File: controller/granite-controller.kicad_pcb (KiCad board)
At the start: 4 copper layers, 199 x 50 mm, 207 parts, among them J1 HR911105A, J10 DRY_IN, J11 MB01_FP, J12 MB02_FP, J13 MB03_FP, J14 MB04_FP, J15 MB05_FP, J16 MB06_FP, J17 MB07_FP, J18 MB08_FP, J2 TYPE-C-31-M-12, J3 19V_IN, J4 1WIRE, J5 1WIRE, J6 1WIRE, J7 1WIRE, J8 EXPANSION, J9 I2C_SENSOR, K1 TLP176AM, K10 TLP176AM, K11 TLP176AM, K12 TLP176AM, K13 TLP176AM, K14 TLP176AM, K15 TLP176AM, K16 TLP176AM, K2 TLP176AM, K3 TLP176AM, K4 TLP176AM, K5 TLP176AM, K6 TLP176AM, K7 TLP176AM, K8 TLP176AM, K9 TLP176AM, U1 ESP32-C6-WROOM-1-N8, U14 MCP23017-E/SO, U15 MCP23017-E/SO, U16 TLP290-4, U17 TLP290-4, U18 TPD4E05U06DQA, U2 TLV62569DBV, U3 W5500, U4 USBLC6-2SC6, U5 TMP1075D, U6 TPD4E05U06DQA, U7 TPD4E05U06DQA, U8 LMR51430YDDCR, Y2 25MHz 12pF YXC

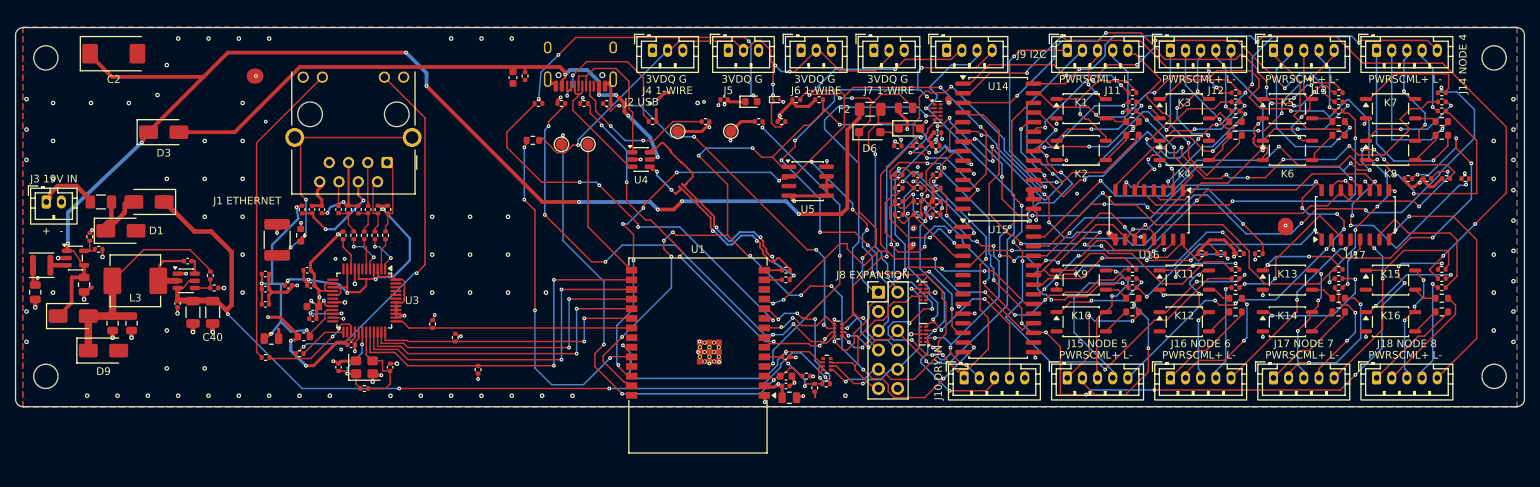
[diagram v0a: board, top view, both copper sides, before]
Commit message: controller rev D: board rebuilt from the rev D schematic and placed, 100 x 50 mm (not routed)
pcbkit mkboard + outline (100 x 50 at rev C's origin, M3 holes in the
corners as rev C), then tools/place.py: ETH (J1 / U3 / Y2 / magnetics,
pairs), buck (U8 loop + U2) and USB-C (J2 / U4) blocks moved from rev C
with their routing (group hand), U1 12 mm left with its decoupling and
antenna still over the bottom edge; probes J4-J7 on the top edge between
RJ45 and USB-C, J11 / J12 (12 V) and J14 / J13 (plane link) on the bottom
edge next to U1's plane I2C pins, J9 / J10 on the right edge. Rule areas:
U1 body, screw heads. Net classes: PWR_19V and node classes gone, PWR_12V
(VIN_12V, 12V_IN_*), LINK?_3V3 in PWR_3V3; pcbkit.toml updated (outline,
classes, labels, KRT nets, keep_groups). DRC parity 0.
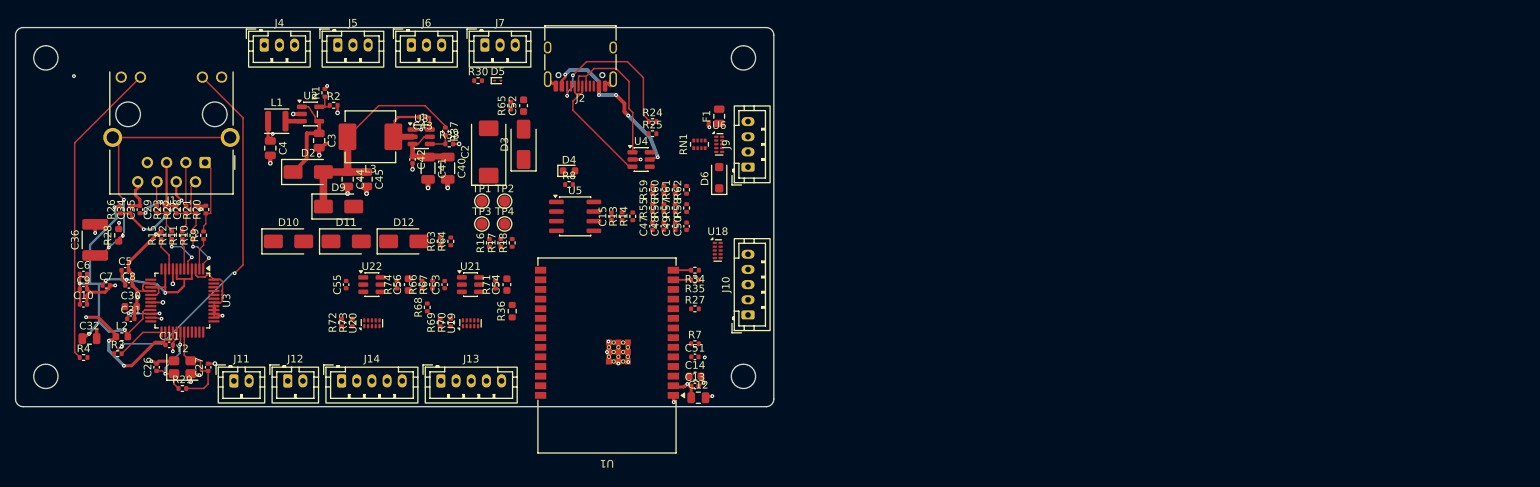
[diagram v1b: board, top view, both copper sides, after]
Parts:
- removed C38, C46: 100n, Capacitor_SMD:C_0402_1005Metric
- removed D1: SMAJ22A, Diode_SMD:D_SMA
- removed D7: SMF5.0A, Diode_SMD:D_SOD-123F
- removed D8: SS34, Diode_SMD:D_SMA
- removed F2: PTC 500mA, Fuse:Fuse_1206_3216Metric
- removed F3: PTC 0.75A, Fuse:Fuse_1206_3216Metric
- removed J15: MB05_FP, Connector_JST:JST_PH_B5B-PH-K_1x05_P2.00mm_Vertical
- removed J16: MB06_FP, Connector_JST:JST_PH_B5B-PH-K_1x05_P2.00mm_Vertical
- removed J17: MB07_FP, Connector_JST:JST_PH_B5B-PH-K_1x05_P2.00mm_Vertical
- removed J18: MB08_FP, Connector_JST:JST_PH_B5B-PH-K_1x05_P2.00mm_Vertical
- removed J3: 19V_IN, Connector_JST:JST_PH_B2B-PH-K_1x02_P2.00mm_Vertical
- removed J8: EXPANSION, Connector_PinHeader_2.54mm:PinHeader_2x06_P2.54mm_Vertical
- removed K1, K10, K11, K12, K13, K14, K15, K16, K2, K3, K4, K5, K6, K7, K8, K9: TLP176AM, Package_SO:SOIC-4_4.55x3.7mm_P2.54mm
- removed R101, R102, R103, R104, R105, R106, R107, R108, R109, R110, R111, R112, R113, R114, R115, R116: 270, Resistor_SMD:R_0402_1005Metric
- removed R19, R32, R33: 10k, Resistor_SMD:R_0402_1005Metric
- removed R201, R202, R203, R204, R205, R206, R207, R208, R209, R210, R211, R212, R213, R214, R215, R216: 100, Resistor_SMD:R_0603_1608Metric
- removed R39, R40, R41, R42, R43, R44, R45, R46: 47k, Resistor_SMD:R_0402_1005Metric
- removed R47, R48, R49, R50, R51, R52, R53, R54: 220, Resistor_SMD:R_0402_1005Metric
- removed R5, R6: 4.7k, Resistor_SMD:R_0402_1005Metric
- removed RN2: 4x330, Resistor_SMD:R_Array_Convex_4x0402
- removed U14, U15: MCP23017-E/SO, Package_SO:SOIC-28W_7.5x17.9mm_P1.27mm
- removed U16, U17: TLP290-4, Package_SO:SOP-16_4.55x10.3mm_P1.27mm
- removed U7: TPD4E05U06DQA, Package_SON:USON-10_2.5x1.0mm_P0.5mm
- added C53: 100n, Capacitor_SMD:C_0402_1005Metric, F.Cu at (81.6, 62.5)
- added C54: 1u, Capacitor_SMD:C_0603_1608Metric, F.Cu at (89.8, 62.5)
- added C55: 100n, Capacitor_SMD:C_0402_1005Metric, F.Cu at (68.6, 62.5)
- added C56: 1u, Capacitor_SMD:C_0603_1608Metric, F.Cu at (76.8, 62.5)
- added D10: SS34, Diode_SMD:D_SMA, F.Cu at (61.0, 56.8)
- added D11: SS34, Diode_SMD:D_SMA, F.Cu at (68.6, 56.8)
- added D12: SMAJ15A, Diode_SMD:D_SMA, F.Cu at (76.2, 56.8)
- added R66: 2.2k, Resistor_SMD:R_0402_1005Metric, F.Cu at (78.6, 62.5)
- added R67: 2.2k, Resistor_SMD:R_0402_1005Metric, F.Cu at (80.0, 62.5)
- added R68: 10k, Resistor_SMD:R_0402_1005Metric, F.Cu at (79.3, 65.5)
- added R69: 33, Resistor_SMD:R_0402_1005Metric, F.Cu at (81.0, 67.5)
- added R70: 33, Resistor_SMD:R_0402_1005Metric, F.Cu at (82.4, 67.5)
- added R71: 180k, Resistor_SMD:R_0402_1005Metric, F.Cu at (88.3, 62.5)
- added R72: 33, Resistor_SMD:R_0402_1005Metric, F.Cu at (68.0, 67.5)
- added R73: 33, Resistor_SMD:R_0402_1005Metric, F.Cu at (69.4, 67.5)
- added R74: 180k, Resistor_SMD:R_0402_1005Metric, F.Cu at (75.3, 62.5)
- added U19: TPD4E05U06DQA, Package_SON:USON-10_2.5x1.0mm_P0.5mm, F.Cu at (85.0, 67.6)
- added U20: TPD4E05U06DQA, Package_SON:USON-10_2.5x1.0mm_P0.5mm, F.Cu at (72.0, 67.6)
- added U21: TPS2553DBVR, Package_TO_SOT_SMD:SOT-23-6, F.Cu at (85.0, 62.5)
- added U22: TPS2553DBVR, Package_TO_SOT_SMD:SOT-23-6, F.Cu at (72.0, 62.5)
- J11: value MB01_FP -> 12V_IN_A; footprint Connector_JST:JST_PH_B5B-PH-K_1x05_P2.00mm_Vertical -> Connector_JST:JST_PH_B2B-PH-K_1x02_P2.00mm_Vertical
- J12: value MB02_FP -> 12V_IN_B; footprint Connector_JST:JST_PH_B5B-PH-K_1x05_P2.00mm_Vertical -> Connector_JST:JST_PH_B2B-PH-K_1x02_P2.00mm_Vertical
- J13: value MB03_FP -> PLANE_LINK_A
- J14: value MB04_FP -> PLANE_LINK_B
- R63: value 100k -> 68k
- moved J14 143.3 mm to (68.0, 75.2)
- moved J12 124.3 mm to (60.9, 75.2)
- moved J11 118.2 mm to (53.8, 75.2)
- moved J13 118.1 mm to (81.1, 75.2)
- moved H2 99.0 mm to (121.0, 32.6)
- moved H3 99.0 mm to (121.0, 74.6)
- moved R63 54.3 mm to (81.0, 56.8), turned to 90 degrees
- moved R64 51.7 mm to (82.4, 56.8), turned to 90 degrees
- moved J5 51.5 mm to (67.5, 30.9)
- moved J6 51.4 mm to (77.2, 30.9)
- moved J7 51.3 mm to (86.9, 30.9)
- moved J4 51.2 mm to (57.8, 30.9)
- moved C2 51.1 mm to (87.4, 45.0), turned to 90 degrees
- moved D3 47.5 mm to (92.0, 44.0), turned to 90 degrees
- moved R30 40.4 mm to (86.0, 35.6)
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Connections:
- net /Expansion header/DRYC1 renamed /Sensors and dry contacts/DRYC1
- net /Expansion header/DRYC2 renamed /Sensors and dry contacts/DRYC2
- net /Expansion header/DRYC3 renamed /Sensors and dry contacts/DRYC3
- net /Expansion header/DRYC4 renamed /Sensors and dry contacts/DRYC4
- net /Expansion header/HDR_3V3 renamed /Sensors and dry contacts/HDR_3V3
- net /Expansion header/HDR_SCL renamed /Sensors and dry contacts/HDR_SCL
- net /Expansion header/HDR_SDA renamed /Sensors and dry contacts/HDR_SDA
- net /Power/VIN_19V renamed /Power/VIN_12V
- J11 pad 1: /Relay channels/MB1_PWR_B -> /Power/12V_IN_A
- J11 pad 2: /Relay channels/MB1_RST_B -> GND
- J12 pad 1: /Relay channels/MB2_PWR_B -> /Power/12V_IN_B
- J12 pad 2: /Relay channels/MB2_RST_B -> GND
- J13 pad 1: /Relay channels/MB3_PWR_B -> /Plane link/LINKA_3V3
- J13 pad 2: /Relay channels/MB3_RST_B -> GND
- J13 pad 3: /Relay channels/MB3_COM -> /Plane link/LINKA_SCL
- J13 pad 4: /Relay channels/MB3_PLED_P -> /Plane link/LINKA_SDA
- J13 pad 5: /Relay channels/MB3_PLED_N -> EXP_INT
- J14 pad 1: /Relay channels/MB4_PWR_B -> /Plane link/LINKB_3V3
- J14 pad 2: /Relay channels/MB4_RST_B -> GND
- J14 pad 3: /Relay channels/MB4_COM -> /Plane link/LINKB_SCL
- J14 pad 4: /Relay channels/MB4_PLED_P -> /Plane link/LINKB_SDA
- J14 pad 5: /Relay channels/MB4_PLED_N -> EXP_INT
- R13 pad 2: I2C_EXT_SCL -> I2C_LOC_SCL
- R14 pad 2: I2C_EXT_SDA -> I2C_LOC_SDA
- RN1 pad 3: /Expansion header/HDR_nRESET -> unconnected-(RN1-R3.1-Pad3)
- RN1 pad 4: /Expansion header/HDR_INT -> unconnected-(RN1-R4.1-Pad4)
- RN1 pad 5: EXP_INT -> unconnected-(RN1-R4.2-Pad5)
- RN1 pad 6: EXP_nRESET -> unconnected-(RN1-R3.2-Pad6)
- RN1 pad 7: I2C_EXT_SDA -> I2C_LOC_SDA
- RN1 pad 8: I2C_EXT_SCL -> I2C_LOC_SCL
- U1 pad 11: EXP_nRESET_INT -> DRY_IN1
- U1 pad 12: unconnected-(U1-IO11-Pad12) -> DRY_IN2
- U1 pad 23: GPIO_IO15 -> DRY_IN4
- U1 pad 26: I2C_INT_SCL -> PLANE_SCL
- U1 pad 27: I2C_INT_SDA -> PLANE_SDA
- U1 pad 4: EXP_nRESET -> DRY_IN3
- U1 pad 6: I2C_EXT_SDA -> I2C_LOC_SDA
- U1 pad 7: I2C_EXT_SCL -> I2C_LOC_SCL
- U5 pad 1: I2C_INT_SDA -> I2C_LOC_SDA
- U5 pad 2: I2C_INT_SCL -> I2C_LOC_SCL
- U6 pad 4: /Expansion header/HDR_nRESET -> unconnected-(U6-D2+-Pad4)
- U6 pad 5: /Expansion header/HDR_INT -> unconnected-(U6-D2--Pad5)
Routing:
- net +5V: track 171.1 -> 11.4 mm, vias 8 -> 0
- net I2C_INT_SDA: track 150.4 -> 0.00 mm, vias 16 -> 0
- net I2C_INT_SCL: track 133.7 -> 0.00 mm, vias 14 -> 0
- net /Power/VIN_12V: track 118.3 -> 8.93 mm, vias 4 -> 0
- net /Relay channels/RST_DRV8: track 105.4 -> 0.00 mm, vias 10 -> 0
- net /Relay channels/RST_DRV4: track 103.9 -> 0.00 mm, vias 4 -> 0
- net EXP_INT: track 100.9 -> 0.00 mm, vias 14 -> 0
- net /Relay channels/NODE_ON5: track 96.4 -> 0.00 mm, vias 10 -> 0
- net /Relay channels/PWR_DRV8: track 96.0 -> 0.00 mm, vias 4 -> 0
- net EXP_nRESET_INT: track 94.3 -> 0.00 mm, vias 6 -> 0
- net GND: track 192.7 -> 99.5 mm, vias 157 -> 36
- net /Relay channels/NODE_ON8: track 87.4 -> 0.00 mm, vias 6 -> 0
- net /Relay channels/PWR_DRV7: track 81.1 -> 0.00 mm, vias 6 -> 0
- net /Sensors and dry contacts/DRYC2: track 77.5 -> 0.00 mm, vias 11 -> 0
- net /Sensors and dry contacts/HDR_SCL: track 77.4 -> 0.00 mm, vias 8 -> 0
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- removed copper zone on In2.Cu, net +3V3
- removed copper zone on B.Cu, net GND
- removed copper zone on F.Cu, net GND
- removed copper zone on In1.Cu, net GND
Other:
- board size 199 x 50 mm -> 100 x 50 mm
- board text removed: "+"
- board text removed: "-"
- board text removed: "3V"
- board text removed: "CM"
- board text removed: "DQ"
- board text removed: "G"
- board text removed: "J1 ETHERNET"
- board text removed: "J10 DRY IN"
- board text removed: "J11"
- board text removed: "J12"
- board text removed: "J13"
- board text removed: "J14 NODE 4"
- board text removed: "J15 NODE 5"
- board text removed: "J16 NODE 6"
- board text removed: "J17 NODE 7"
- board text removed: "J18 NODE 8"
- board text removed: "J2 USB"
- board text removed: "J3 19V IN"
- board text removed: "J4 1-WIRE"
- board text removed: "J5"
- board text removed: "J6 1-WIRE"
- board text removed: "J7 1-WIRE"
- board text removed: "J8 EXPANSION"
- board text removed: "J9 I2C"
- board text removed: "L+"
- board text removed: "L-"
- board text removed: "PW"
- board text removed: "RS"

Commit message: controller rev D: board widened to 105 x 50 mm, SPI bus and plane I2C escapes hand-routed (tools/route_hand.py)
At 100 mm the bottom edge was full (J11 / J12 / J14 / J13 end 1.3 mm
from U1) and the SPI via column and the plane I2C escapes had to sit
over J13's pins. U1 (dx -7 from rev C), USB-C (+5) and everything right
of the buck move 5 mm right; the U1 body keep-out moves with U1.
route_hand.py: rev C's W5500 SPI bus (F.Cu at 0.8 mm pitch, via column
x 92.6 - 96.6 between J13 and U1, B.Cu up to U1's pins, RST straight on
F.Cu) and PLANE_SCL / PLANE_SDA from U1 pins 26 / 27 to vias at
(91.2, 73.85) / (90.2, 73.85), all in group hand. Pull-ups R17 / R18 on
the INT / RST lines as rev C. DRC parity 0, not routed otherwise.
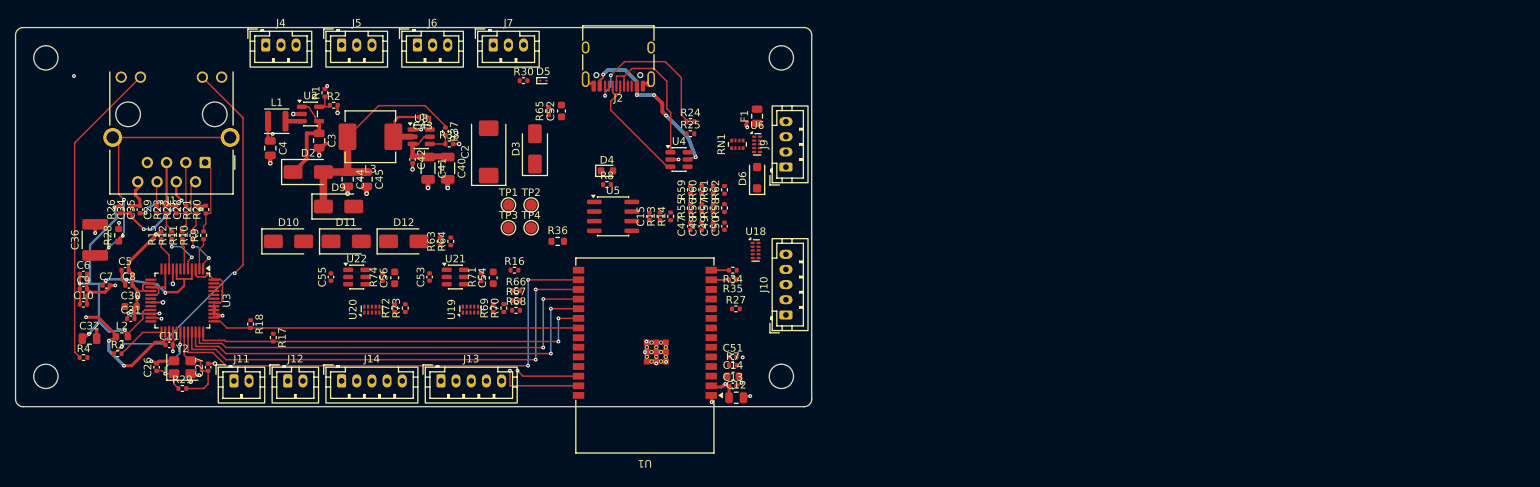
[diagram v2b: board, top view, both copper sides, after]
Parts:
- moved R18 36.1 mm to (56.0, 67.7), turned to -90 degrees
- moved R17 32.5 mm to (59.0, 69.5), turned to -90 degrees
- moved R66 12.4 mm to (91.0, 63.3), turned to 0 degrees
- moved R68 11.7 mm to (91.0, 65.9), turned to 0 degrees
- moved R67 11.2 mm to (91.0, 64.6), turned to 0 degrees
- moved R36 11.0 mm to (96.5, 56.8), turned to 0 degrees
- moved R69 7.25 mm to (88.0, 65.6)
- moved R70 7.25 mm to (89.4, 65.6)
- moved R72 7.25 mm to (75.0, 65.6)
- moved R73 7.25 mm to (76.4, 65.6)
- moved D5 6.00 mm to (94.6, 35.6)
- moved R30 6.00 mm to (92.0, 35.6)
- moved R7 5.76 mm to (119.6, 73.2)
- moved R27 5.40 mm to (120.0, 65.7)
- moved C52 5.05 mm to (97.0, 39.6)
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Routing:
- net ETH_CS: track 0.00 -> 66.2 mm, vias 0 -> 2
- net ETH_SCLK: track 0.00 -> 63.1 mm, vias 0 -> 2
- net ETH_MISO: track 0.00 -> 58.7 mm, vias 0 -> 2
- net ETH_MOSI: track 0.00 -> 58.1 mm, vias 0 -> 2
- net ETH_INT: track 0.00 -> 53.7 mm, vias 0 -> 2
- net ETH_RST: track 0.00 -> 48.4 mm
- net PLANE_SDA: track 0.00 -> 11.0 mm, vias 0 -> 1
- net PLANE_SCL: track 0.00 -> 8.35 mm, vias 0 -> 1
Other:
- board size 100 x 50 mm -> 105 x 50 mm

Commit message: controller rev D: placement reworked for routing (105 x 50 mm, not routed)
tools/place.py: J10 top right with one RC row per pin at the pin's y
(C | 1k | 10k pull-up on the DRYC line), U18 below it; J9 lower right
with U6, RN1, F1, D6; R34 / R35 back beside U1's USB pins (rev C), the
USB pair runs down from U4 clear of the RC rows; rev C's board-only 3D
models (J1, J2) copied with the blocks; +3V3 hand copper not copied
(krt-route's plane pass drops it), nothing copied under the screw heads.
tools/route_hand.py: also the J10 row shorts with their plane vias and
a GND strap + plane via on each TPD4E05U06 (pads 3 / 8); --only NET
re-applies the SPI / RST routes after krt-route. DRC parity 0.

The TLP176AM / TLP290-4 STEP files (K1-K16, U16 / U17 are gone) and
their 3dmodels/README.md rows removed.
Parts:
- moved F1 26.5 mm to (121.4, 66.8)
- moved D6 21.4 mm to (121.0, 69.8), turned to 0 degrees
- moved J9 21.0 mm to (126.6, 68.0)
- moved RN1 18.9 mm to (122.0, 62.8), turned to 180 degrees
- moved J10 17.5 mm to (126.6, 49.0)
- moved U6 14.0 mm to (123.2, 58.0)
- moved R27 12.0 mm to (112.6, 56.2), turned to 90 degrees
- moved C50 11.9 mm to (117.2, 43.0), turned to 180 degrees
- moved C49 9.80 mm to (117.2, 45.0), turned to 180 degrees
- moved R58 9.44 mm to (119.4, 43.0), turned to 0 degrees
- moved R62 8.12 mm to (121.6, 42.5), turned to -90 degrees
- moved C48 7.98 mm to (117.2, 47.0), turned to 180 degrees
- moved R57 7.78 mm to (119.4, 45.0), turned to 0 degrees
- moved R59 7.75 mm to (121.6, 48.5), turned to -90 degrees
- moved R61 7.18 mm to (121.6, 44.5), turned to -90 degrees
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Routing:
- net +3V3: track 28.3 -> 5.27 mm, vias 6 -> 5
- net PLANE_SDA: track 11.0 -> 0.00 mm, vias 1 -> 0
- net PLANE_SCL: track 8.35 -> 0.00 mm, vias 1 -> 0
- net GND: track 99.6 -> 107.6 mm, vias 36 -> 43
- net /Sensors and dry contacts/DRYC4: track 0.00 -> 6.69 mm
- net /Sensors and dry contacts/DRYC3: track 0.00 -> 6.69 mm
- net /Sensors and dry contacts/DRYC2: track 0.00 -> 6.69 mm
- net /Sensors and dry contacts/DRYC1: track 0.00 -> 6.69 mm
- net DRY_IN4: track 0.00 -> 1.21 mm
- net DRY_IN3: track 0.00 -> 1.21 mm
- net DRY_IN2: track 0.00 -> 1.21 mm
- net DRY_IN1: track 0.00 -> 1.21 mm

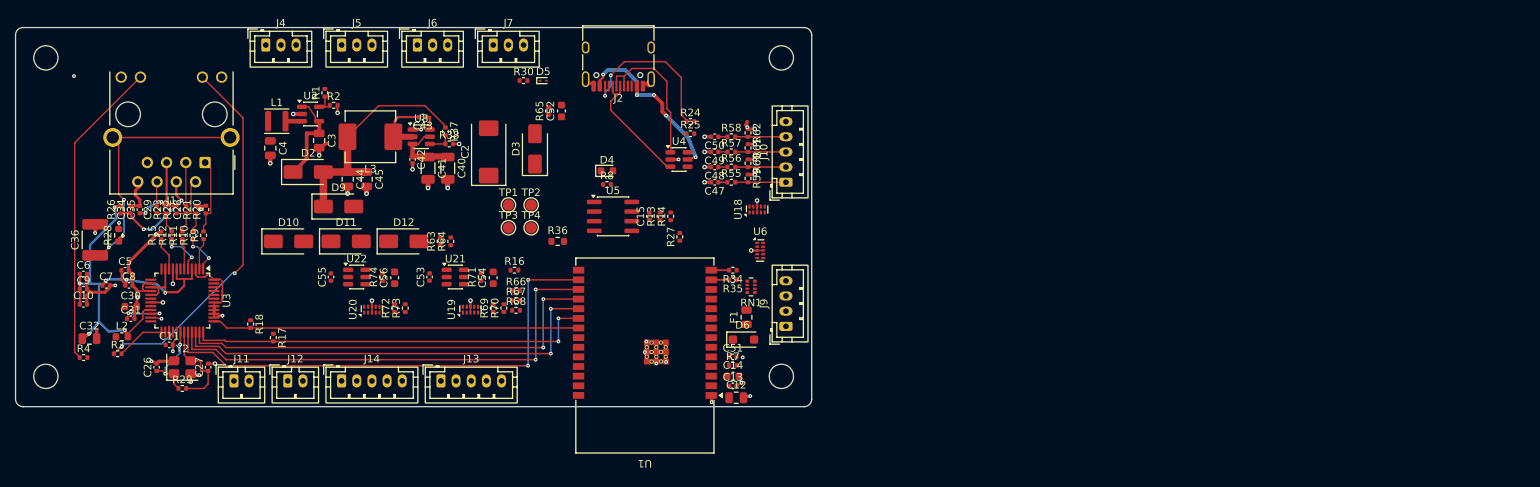
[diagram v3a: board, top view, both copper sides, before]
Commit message: controller rev D: routed, DRC 0 errors, 0 unconnected, parity clean (105 x 50 mm)
Kept from rev C (group hand): Ethernet block with the MDI pairs, magnetics
network, crystal and W5500 decoupling; buck U8 loop and U2; USB-C J2 / U4;
U1 thermal vias. Hand routes (tools/route_hand.py): W5500 SPI bus and RST,
J10 RC rows, ESD GND straps, U21 / U22 load-switch fan-out (IN / EN loop,
GND via under the body, ILIM). Rest by krt-route (planes GND In1 / +3V3
In2, USB pair U4 -> R34 / R35, signals F / B), then tools/restore_hand.py
(krt-route ripped ETH_XI and part of the hand GND; put back, duplicate
vias merged), targeted krt-reroute --keep passes on the opens (VIN_SENSE,
DRY_IN3, I2C_LOC_SDA, C6_EN, 12V_IN_B, LINKA / LINKB_3V3, ETH_LED_ACT,
OW_MCU, EXP_INT, HDR_SDA), prune, viaout; GND pours F / B with 40
stitching vias; J2 shield pads solid to the pour (a starved thermal
otherwise); silk and connector labels (J9 and J7 pin legends found no
room). DRC: 0 errors, 0 unconnected, 0 parity; 4 silk-edge warnings from
the J2 and U1 overhangs as on rev C. No tracks on In1 / In2; vias in SMD
pads only U1's 4 thermal vias.
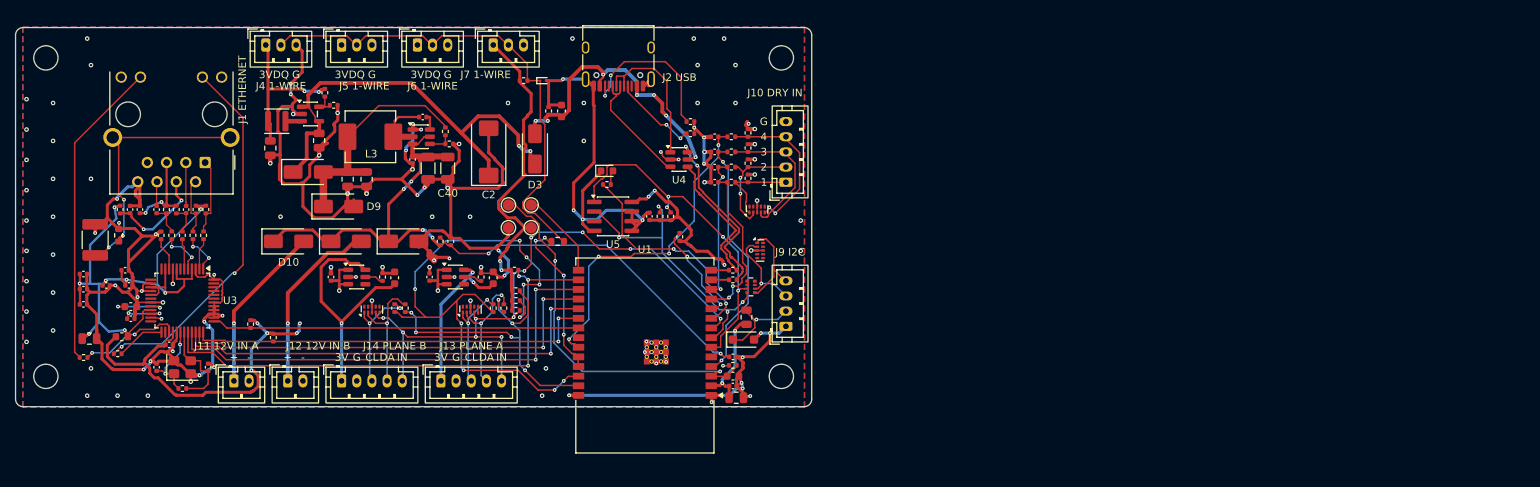
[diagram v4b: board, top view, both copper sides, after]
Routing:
- net GND: track 107.6 -> 466.5 mm, vias 43 -> 113
- net +3V3: track 5.27 -> 175.2 mm, vias 5 -> 22
- net EXP_INT: track 0.00 -> 83.0 mm, vias 0 -> 11
- net PLANE_SCL: track 0.00 -> 79.7 mm, vias 0 -> 10
- net /MCU/OW_DATA: track 0.00 -> 65.5 mm
- net /MCU/C6_EN: track 0.00 -> 49.9 mm, vias 0 -> 2
- net VIN_SENSE: track 0.00 -> 46.1 mm, vias 0 -> 2
- net I2C_LOC_SDA: track 0.00 -> 45.6 mm, vias 0 -> 4
- net +5V: track 11.4 -> 56.7 mm, vias 0 -> 2
- net PLANE_SDA: track 0.00 -> 43.9 mm, vias 0 -> 6
- net DRY_IN4: track 1.21 -> 42.5 mm, vias 0 -> 4
- net I2C_LOC_SCL: track 0.00 -> 37.5 mm, vias 0 -> 4
- net /Power/VIN_12V: track 8.93 -> 45.2 mm, vias 0 -> 4
- net /Plane link/LINKB_3V3: track 0.00 -> 31.8 mm, vias 0 -> 1
- net DRY_IN3: track 1.21 -> 32.8 mm, vias 0 -> 2
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- added copper zone on In2.Cu, net +3V3
- added copper zone on B.Cu, net GND
- added copper zone on F.Cu, net GND
- added copper zone on In1.Cu, net GND
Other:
- board text added: "+"
- board text added: "-"
- board text added: "1"
- board text added: "2"
- board text added: "3"
- board text added: "3V"
- board text added: "4"
- board text added: "CL"
- board text added: "DA"
- board text added: "DQ"
- board text added: "G"
- board text added: "IN"
- board text added: "J1 ETHERNET"
- board text added: "J10 DRY IN"
- board text added: "J11 12V IN A"
- board text added: "J12 12V IN B"
- board text added: "J13 PLANE A"
- board text added: "J14 PLANE B"
- board text added: "J2 USB"
- board text added: "J4 1-WIRE"
- board text added: "J5 1-WIRE"
- board text added: "J6 1-WIRE"
- board text added: "J7 1-WIRE"
- board text added: "J9 I2C"
